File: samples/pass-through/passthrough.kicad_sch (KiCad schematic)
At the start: 12 parts, among them J1 Conn_01x04_Pin, J2 Conn_01x04_Pin, U2 FPC-05FB-12PH20, U3 FPC-05FB-12PH20, U4 BSS138_C7420339, U5 BSS138_C7420339

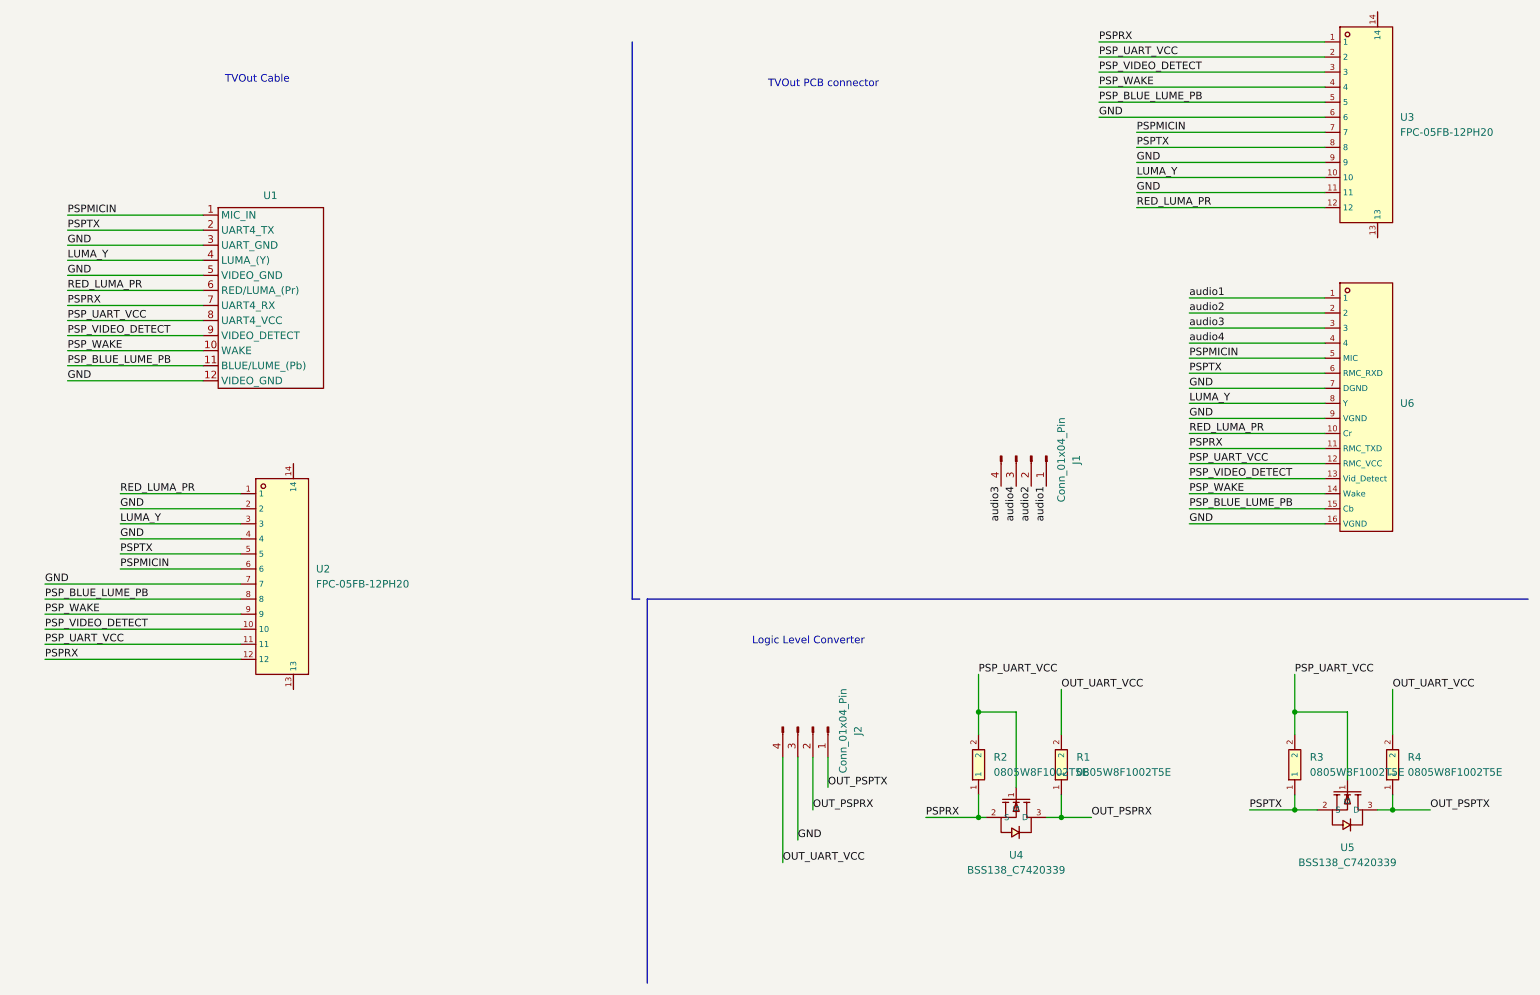
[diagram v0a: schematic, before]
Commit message: restructure and widen tvout connector
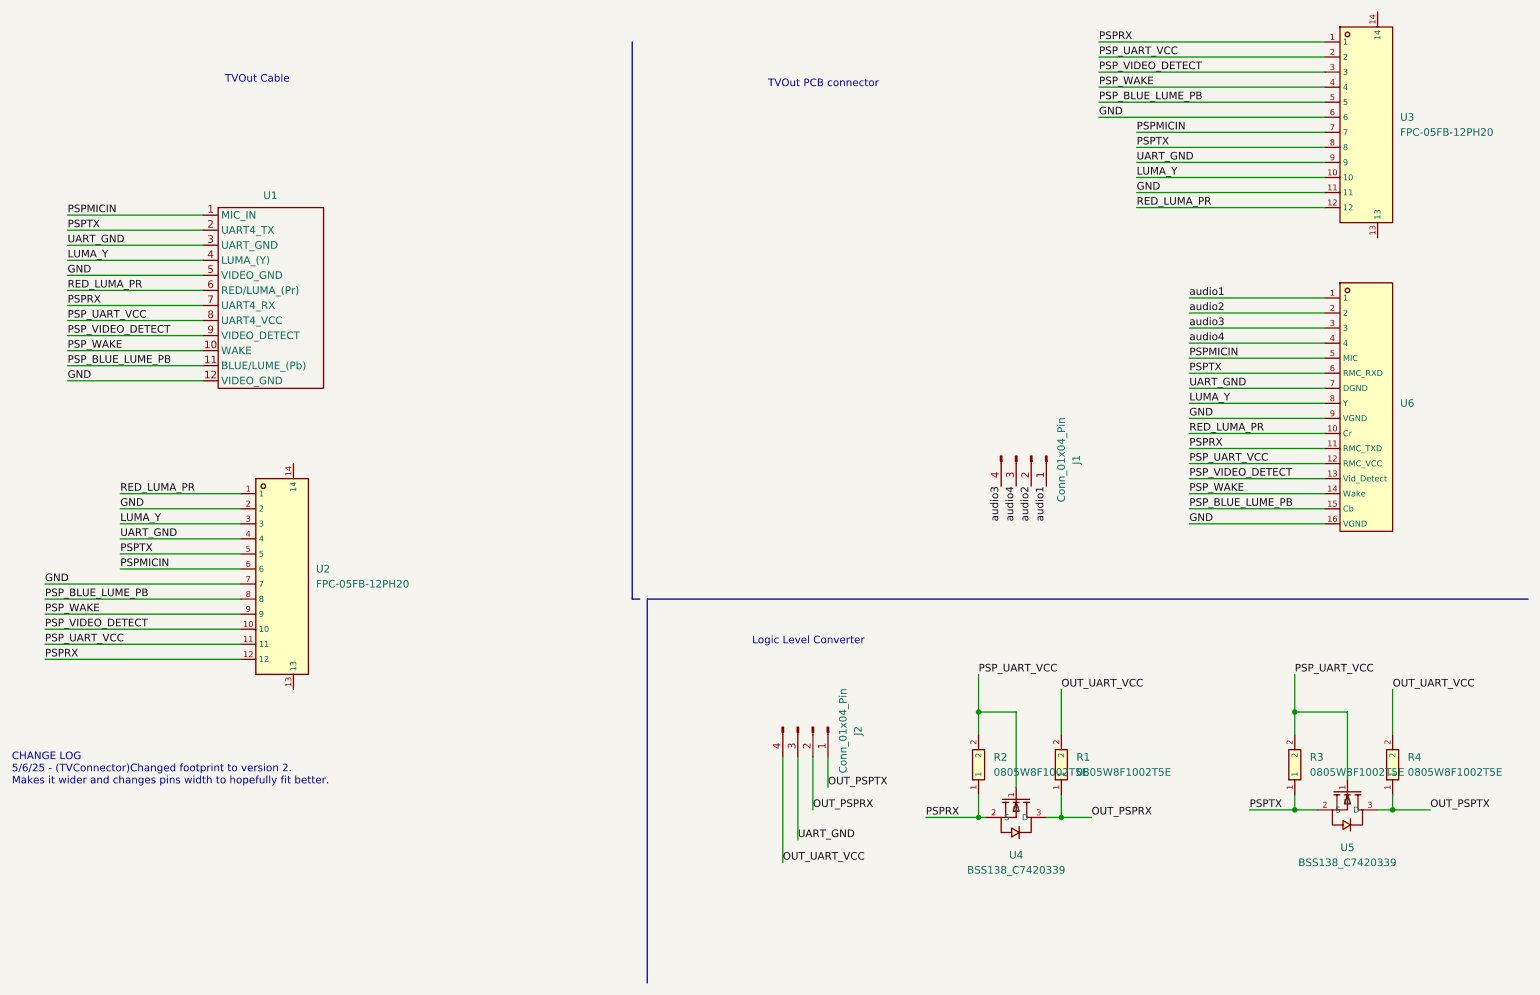
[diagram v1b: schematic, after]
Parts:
- U1: symbol psp2:tvout cable -> psp:tvout cable
- U6: symbol psp2:tvoutConnector -> psp:tvoutConnector
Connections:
- net GND: no longer J2.3 (Pin_3), U1.3 (UART_GND), U2.4, U3.9, U6.7 (DGND)
- new net UART_GND: J2.3 (Pin_3), U1.3 (UART_GND), U2.4, U3.9, U6.7 (DGND)
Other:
- note added: "CHANGE LOG 5/6/25 - (TVConnector)Changed footprint to version 2. Makes it wider and changes pins width to hopefully fit better."
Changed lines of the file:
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@@
+		)
+	)
+	(text "CHANGE LOG\n5/6/25 - (TVConnector)Changed footprint to version 2. \nMakes it wider and changes pins width to hopefully fit better."
+		(exclude_from_sim no)
+		(at 21.082 143.002 0)
+		(effects
+			(font
+				(size 1.27 1.27)
+			)
+			(justify left)
 		)
 	)
@@
 		)
 	)
+	(label "UART_GND"
+		(at 210.82 40.64 0)
+		(fields_autoplaced yes)
+		(effects
+			(font
+				(size 1.27 1.27)
+			)
+			(justify left bottom)
+		)
+	)
 	(label "PSP_BLUE_LUME_PB"
 		(at 204.47 30.48 0)
@@
 		)
 	)
-	(label "GND"
-		(at 39.37 104.14 0)
+	(label "UART_GND"
+		(at 153.67 154.94 0)
 		(fields_autoplaced yes)
 		(effects
@@
 		)
 	)
-	(label "GND"
-		(at 210.82 40.64 0)
-		(fields_autoplaced yes)
-		(effects
-			(font
-				(size 1.27 1.27)
-			)
-			(justify left bottom)
-		)
-	)
 	(label "PSPMICIN"
 		(at 210.82 35.56 0)
@@
 		)
 	)
-	(label "GND"
+	(label "UART_GND"
+		(at 219.71 78.74 0)
+		(fields_autoplaced yes)
+		(effects
+			(font
+				(size 1.27 1.27)
+			)
+			(justify left bottom)
+		)
+	)
+	(label "UART_GND"
 		(at 30.48 54.61 0)
 		(fields_autoplaced yes)
@@
 		)
 	)
-	(label "GND"
-		(at 153.67 154.94 0)
-		(fields_autoplaced yes)
-		(effects
-			(font
-				(size 1.27 1.27)
-			)
-			(justify left bottom)
-		)
-	)
 	(label "PSP_WAKE"
 		(at 219.71 96.52 0)
@@
 		)
 	)
+	(label "UART_GND"
+		(at 39.37 104.14 0)
+		(fields_autoplaced yes)
+		(effects
+			(font
+				(size 1.27 1.27)
+			)
+			(justify left bottom)
+		)
+	)
 	(label "audio4"
 		(at 219.71 71.12 0)
@@
 		)
 	)
-	(label "GND"
-		(at 219.71 78.74 0)
-		(fields_autoplaced yes)
-		(effects
-			(font
-				(size 1.27 1.27)
-			)
-			(justify left bottom)
-		)
-	)
 	(label "OUT_PSPTX"
 		(at 260.35 149.86 0)
@@
 	)
 	(symbol
-		(lib_id "psp2:tvoutConnector")
+		(lib_id "psp:tvoutConnector")
 		(at 257.81 83.82 0)
 		(unit 1)
@@
 		)
 		(property "Footprint" "psp:TVOut Connector"
-			(at 257.81 83.82 0)
+			(at 267.208 85.344 0)
 			(effects
 				(font
@@
 	)
 	(symbol
-		(lib_id "psp2:tvout cable")
+		(lib_id "psp:tvout cable")
 		(at 73.66 58.42 0)
 		(unit 1)
